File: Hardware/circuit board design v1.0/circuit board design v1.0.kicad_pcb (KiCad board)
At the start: 4 copper layers, 30 x 79.9 mm, 47 parts, among them IC1 BMI088, J1 Conn_01x06_Male, J2 Conn_01x02, J3 105017-0001, J4 Conn_01x04, Q1 2N7002-7-F, U1 STM32F446RETx, U2 W25Q64JVSS, U3 SDR08540M3-01, U4 BME280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

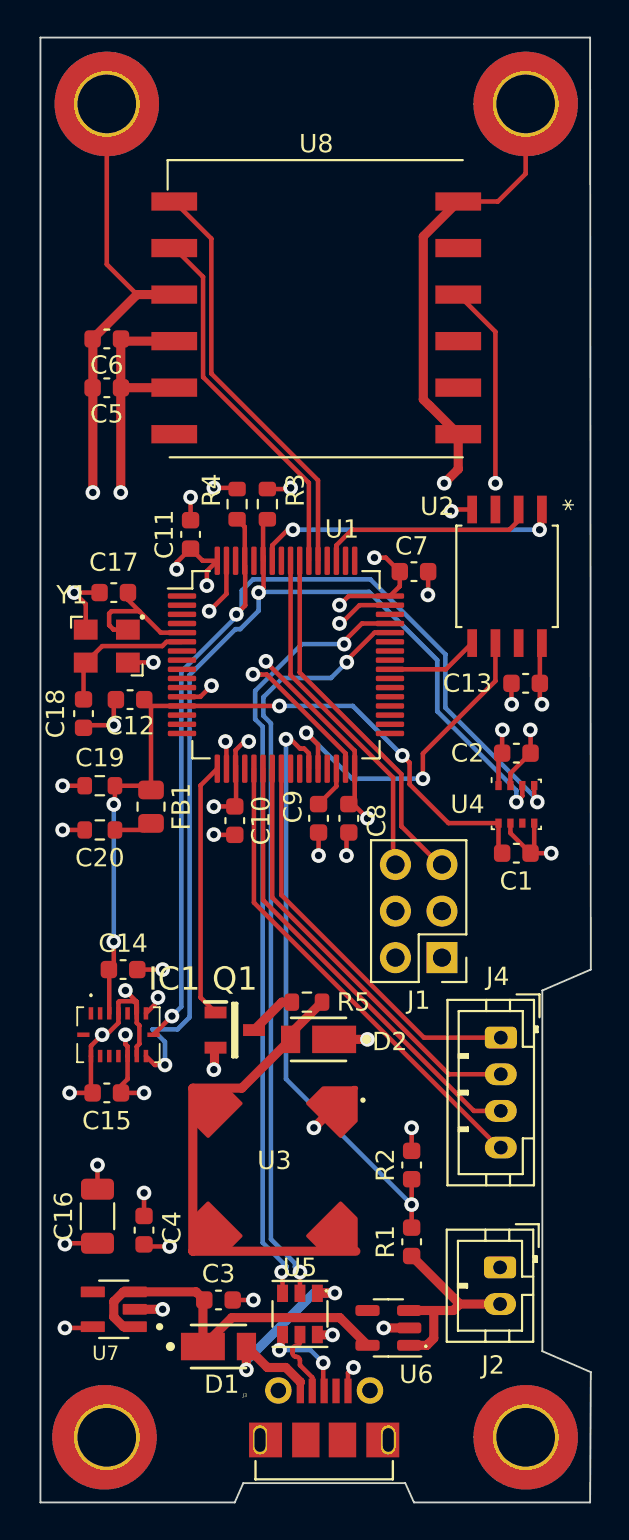
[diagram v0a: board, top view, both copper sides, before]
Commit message: Changed connectors to horizontal
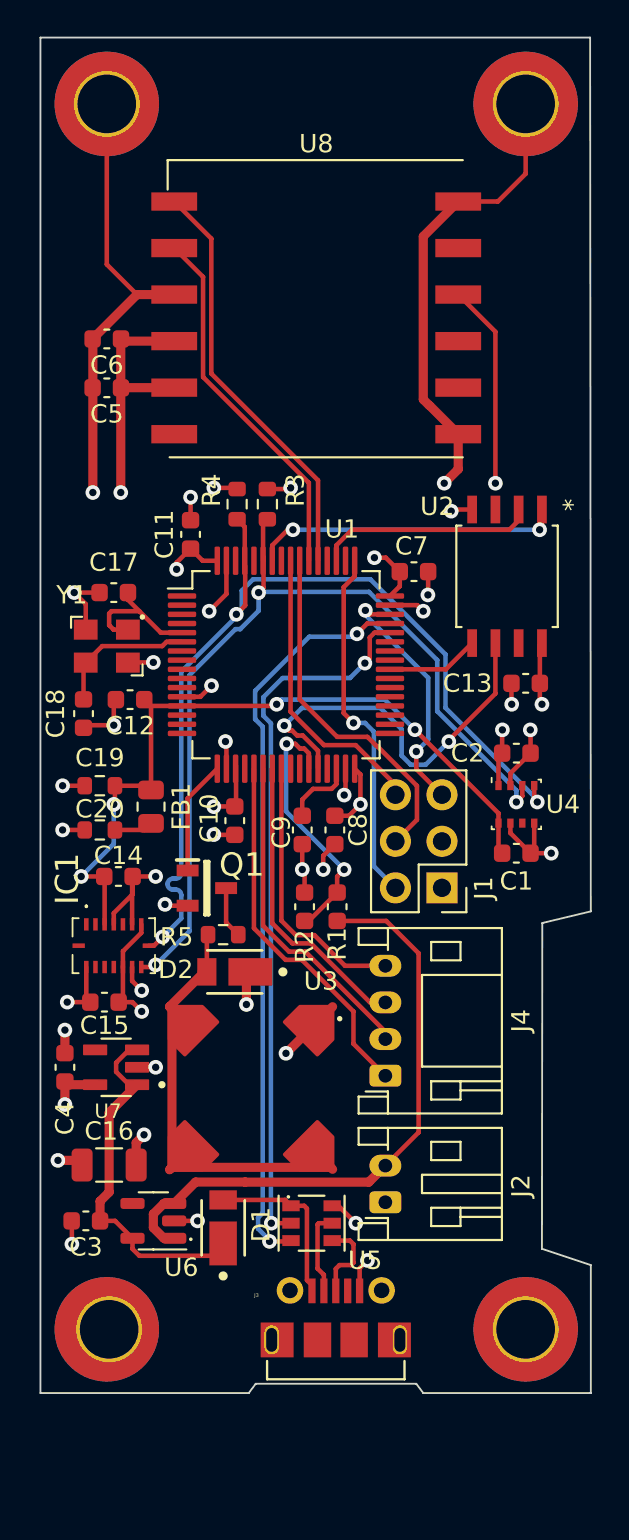
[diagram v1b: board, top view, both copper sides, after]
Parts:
- J2: footprint Components:JST_PH_B2B-PH-K_1x02_P2.00mm_Vertical -> Components:JST_PH_S2B-PH-K_1x02_P2.00mm_Horizontal
- J4: footprint Components:JST_PH_B4B-PH-K_1x04_P2.00mm_Vertical -> Components:JST_PH_S4B-PH-K_1x04_P2.00mm_Horizontal
- moved R1 18.7 mm to (36.2, 67.4)
- moved R2 15.3 mm to (34.4, 67.4)
- moved U6 14.1 mm to (26.2, 84.6)
- moved U7 13.2 mm to (24.1, 76.2)
- moved C4 9.88 mm to (21.3, 76.2)
- moved C3 8.43 mm to (22.5, 84.6), turned to 180 degrees
- moved Q1 7.90 mm to (29.1, 66.4)
- moved J2 7.20 mm to (38.8, 83.6), turned to 90 degrees
- moved J4 6.64 mm to (38.8, 76.7), turned to 90 degrees
- moved D1 6.48 mm to (30.0, 85.0), turned to -90 degrees
- moved H1 5.89 mm to (23.6, 90.5)
- moved H4 5.89 mm to (46.5, 90.5)
- moved D2 5.87 mm to (30.6, 71.0)
- moved R5 5.87 mm to (30.0, 69.0), turned to 0 degrees
- moved J3 5.50 mm to (36.1, 91.1)
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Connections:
- net /MCU/SYS_JTDO-SWO renamed /MCU/SYS_JTDO_SWO
- J1 pad 2: /MCU/SYS_JTCK-SWCLK -> /MCU/SYS_JTCK_SWCLK
- J1 pad 4: /MCU/SYS_JTMS-SWDIO -> /MCU/SYS_JTRST
- J1 pad 5: /MCU/SYS_JTRST -> /MCU/SYS_JTMS_SWDIO
- J4 pad 1: /MCU/Radio_Enable -> /MCU/SPI1_SCK
- J4 pad 2: /MCU/SPI1_MOSI -> /MCU/SPI1_MISO
- J4 pad 3: /MCU/SPI1_MISO -> /MCU/SPI1_MOSI
- J4 pad 4: /MCU/SPI1_SCK -> /MCU/Radio_Enable
- U1 pad 46: /MCU/SYS_JTMS-SWDIO -> /MCU/SYS_JTMS_SWDIO
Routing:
- net Net-(J2-Pad2): track 11.8 -> 33.4 mm
- net /MCU/SYS_JTCK_SWCLK: track 0.00 -> 19.6 mm, vias 0 -> 1
- net /MCU/PWR_BVOLTS: track 33.3 -> 14.3 mm
- net /MCU/SYS_JTMS_SWDIO: track 0.00 -> 13.8 mm, vias 0 -> 2
- net +3.3V: track 77.7 -> 64.5 mm, vias 22 -> 15
- net GND: track 120.9 -> 112.4 mm, vias 34 -> 32
- net /MCU/buzzer_gate: track 14.0 -> 6.23 mm
- net /MCU/SPI1_MOSI: track 23.5 -> 16.4 mm
- net /MCU/Radio_Enable: track 22.1 -> 15.0 mm
- net /MCU/SDA: track 57.0 -> 49.9 mm
- net /MCU/SPI1_MISO: track 24.9 -> 18.0 mm
- net /MCU/SPI1_SCK: track 26.3 -> 20.2 mm
- net Net-(D2-Pad2): track 27.0 -> 22.7 mm
- net VBUS: track 13.3 -> 9.38 mm, vias 2 -> 0
- net /MCU/SCL: track 55.7 -> 52.0 mm
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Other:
- board size 30 x 79.9 mm -> 30 x 74 mm
- board text added: "IC SpaceSoc Flight Computer V1.0 2023"

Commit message: Added extra cap in case its needed
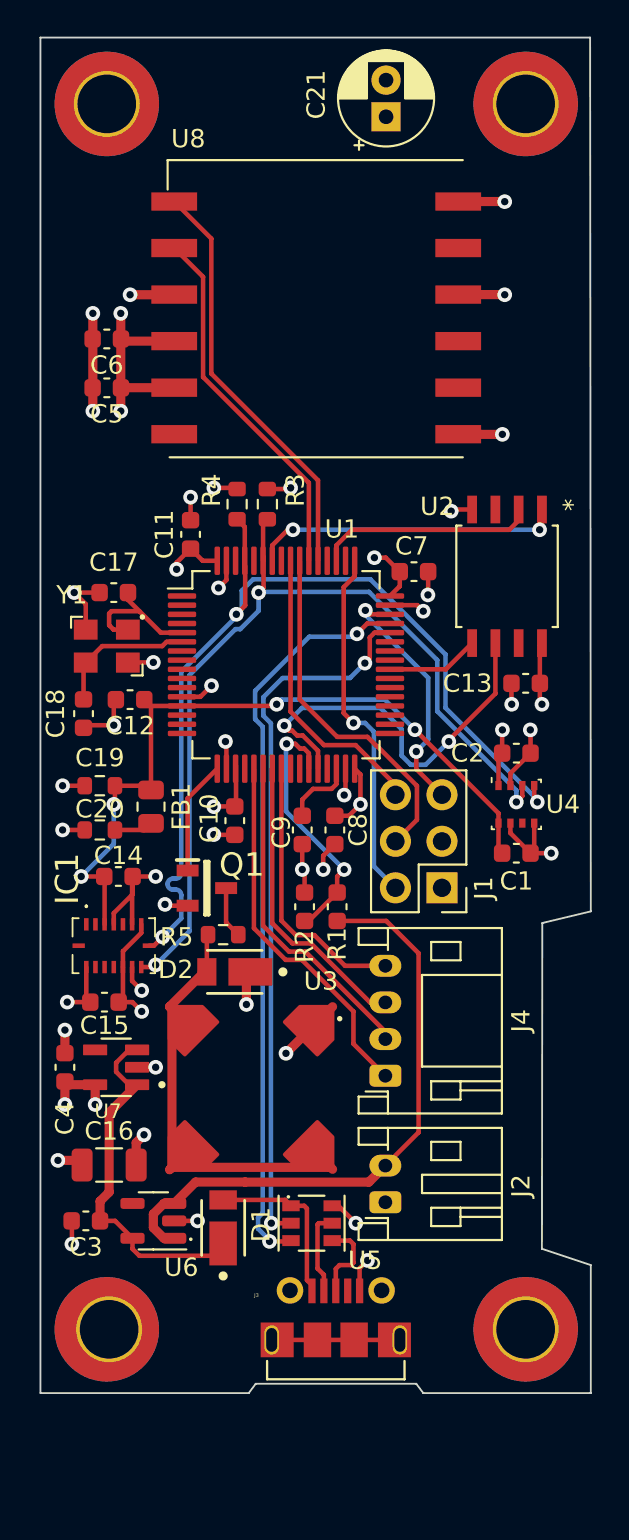
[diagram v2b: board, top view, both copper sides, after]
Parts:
- added C21: 4.7uF, Capacitor_THT:CP_Radial_D5.0mm_P2.00mm, F.Cu at (38.9, 24.3)
- C5: value 100n -> 100nF
- C6: value C_Small -> 100nF
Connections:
- J3 pad P$1: (no net) -> GND
- J3 pad P$10: (no net) -> GND
- J3 pad P$11: (no net) -> GND
- J3 pad P$12: (no net) -> GND
- J3 pad P$13: (no net) -> GND
- J3 pad P$2: (no net) -> GND
- J3 pad P$8: (no net) -> GND
- J3 pad P$9: (no net) -> GND
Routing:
- net GND: track 112.4 -> 79.7 mm, vias 32 -> 35
- net +3.3V: track 64.5 -> 53.8 mm, vias 15 -> 17
